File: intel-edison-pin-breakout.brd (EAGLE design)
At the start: 93.7 x 78.7 mm, 5 parts, among them U1 EDISON_CONNECTOR_FULLMOUNTING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

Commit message: put them closer
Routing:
- net N$33: track 56.3 -> 49.6 mm
- net N$1: track 55.5 -> 50.2 mm
- net N$32: track 53.1 -> 48.1 mm
- net N$2: track 52.4 -> 48.6 mm
- net N$31: track 50.3 -> 46.7 mm
- net N$3: track 49.5 -> 47.1 mm
- net N$30: track 46.9 -> 45.2 mm
- net N$4: track 46.8 -> 45.5 mm
- net N$5: track 44.8 -> 44.1 mm
- net N$29: track 44.5 -> 43.7 mm
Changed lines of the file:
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@@
 <contactref element="JP1" pad="1"/>
 <wire x1="40.52" y1="36.27" x2="40.518078125" y2="35.51681875" width="0.2032" layer="1"/>
-<wire x1="3.81" y1="3.81" x2="3.81" y2="17.78" width="0.2032" layer="1"/>
-<wire x1="3.81" y1="17.78" x2="40.518078125" y2="35.51681875" width="0.2032" layer="1"/>
+<wire x1="3.81" y1="3.81" x2="3.81" y2="6.35" width="0.2032" layer="1"/>
+<wire x1="3.81" y1="6.35" x2="40.518078125" y2="35.51681875" width="0.2032" layer="1"/>
 </signal>
 <signal name="N$2">
@@
 <contactref element="JP1" pad="2"/>
 <wire x1="40.92" y1="36.27" x2="40.9194" y2="35.304728125" width="0.2032" layer="1"/>
-<wire x1="6.35" y1="3.81" x2="6.35" y2="15.24" width="0.2032" layer="1"/>
-<wire x1="6.35" y1="15.24" x2="40.9194" y2="35.304728125" width="0.2032" layer="1"/>
+<wire x1="6.35" y1="3.81" x2="6.35" y2="6.35" width="0.2032" layer="1"/>
+<wire x1="6.35" y1="6.35" x2="40.9194" y2="35.304728125" width="0.2032" layer="1"/>
 </signal>
 <signal name="N$3">
@@
 <contactref element="JP1" pad="3"/>
 <wire x1="41.32" y1="36.27" x2="41.3169125" y2="35.05961875" width="0.2032" layer="1"/>
-<wire x1="8.89" y1="3.81" x2="8.89" y2="12.7" width="0.2032" layer="1"/>
-<wire x1="8.89" y1="12.7" x2="41.3169125" y2="35.05961875" width="0.2032" layer="1"/>
+<wire x1="8.89" y1="3.81" x2="8.89" y2="6.35" width="0.2032" layer="1"/>
+<wire x1="8.89" y1="6.35" x2="41.3169125" y2="35.05961875" width="0.2032" layer="1"/>
 </signal>
 <signal name="N$4">
@@
 <contactref element="JP1" pad="4"/>
 <wire x1="41.72" y1="36.27" x2="41.7068" y2="34.847528125" width="0.2032" layer="1"/>
-<wire x1="11.43" y1="3.81" x2="11.43" y2="10.16" width="0.2032" layer="1"/>
-<wire x1="11.43" y1="10.16" x2="41.7068" y2="34.847528125" width="0.2032" layer="1"/>
+<wire x1="11.43" y1="3.81" x2="11.43" y2="6.35" width="0.2032" layer="1"/>
+<wire x1="11.43" y1="6.35" x2="41.7068" y2="34.847528125" width="0.2032" layer="1"/>
 </signal>
 <signal name="N$5">
@@
 <contactref element="JP1" pad="5"/>
 <wire x1="42.12" y1="36.27" x2="42.1132" y2="34.671" width="0.2032" layer="1"/>
-<wire x1="13.97" y1="3.81" x2="13.97" y2="8.89" width="0.2032" layer="1"/>
-<wire x1="13.97" y1="8.89" x2="42.1132" y2="34.671" width="0.2032" layer="1"/>
+<wire x1="13.97" y1="3.81" x2="13.97" y2="6.35" width="0.2032" layer="1"/>
+<wire x1="13.97" y1="6.35" x2="42.1132" y2="34.671" width="0.2032" layer="1"/>
 </signal>
 <signal name="N$6">
 <contactref element="U1" pad="11"/>
 <contactref element="JP1" pad="6"/>
-<wire x1="16.51" y1="3.81" x2="16.51" y2="7.62" width="0.2032" layer="1"/>
+<wire x1="16.51" y1="3.81" x2="16.51" y2="6.35" width="0.2032" layer="1"/>
 <wire x1="42.52" y1="36.27" x2="42.503090625" y2="34.5059" width="0.2032" layer="1"/>
-<wire x1="42.503090625" y1="34.5059" x2="16.51" y2="7.62" width="0.2032" layer="1"/>
+<wire x1="42.503090625" y1="34.5059" x2="16.51" y2="6.35" width="0.2032" layer="1"/>
 </signal>
 <signal name="N$7">
@@
 <contactref element="JP2" pad="1"/>
 <wire x1="52.52" y1="36.27" x2="52.515771875" y2="34.189671875" width="0.2032" layer="1"/>
-<wire x1="80.01" y1="3.81" x2="80.01" y2="8.89" width="0.2032" layer="1"/>
-<wire x1="80.01" y1="8.89" x2="52.515771875" y2="34.189671875" width="0.2032" layer="1"/>
+<wire x1="80.01" y1="3.81" x2="80.01" y2="6.35" width="0.2032" layer="1"/>
+<wire x1="80.01" y1="6.35" x2="52.515771875" y2="34.189671875" width="0.2032" layer="1"/>
 </signal>
 <signal name="N$30">
@@
 <contactref element="JP2" pad="2"/>
 <wire x1="52.92" y1="36.27" x2="52.925978125" y2="34.4678" width="0.2032" layer="1"/>
-<wire x1="82.55" y1="3.81" x2="82.55" y2="11.43" width="0.2032" layer="1"/>
-<wire x1="52.925978125" y1="34.4678" x2="82.55" y2="11.43" width="0.2032" layer="1"/>
+<wire x1="82.55" y1="3.81" x2="82.55" y2="6.35" width="0.2032" layer="1"/>
+<wire x1="52.925978125" y1="34.4678" x2="82.55" y2="6.35" width="0.2032" layer="1"/>
 </signal>
 <signal name="N$31">
 <contactref element="U1" pad="65"/>
 <contactref element="JP2" pad="3"/>
-<wire x1="85.09" y1="3.81" x2="85.09" y2="15.24" width="0.2032" layer="1"/>
+<wire x1="85.09" y1="3.81" x2="85.09" y2="6.35" width="0.2032" layer="1"/>
 <wire x1="53.32" y1="36.27" x2="53.30570625" y2="34.72815" width="0.2032" layer="1"/>
-<wire x1="53.30570625" y1="34.72815" x2="85.09" y2="15.24" width="0.2032" layer="1"/>
+<wire x1="53.30570625" y1="34.72815" x2="85.09" y2="6.35" width="0.2032" layer="1"/>
 </signal>
 <signal name="N$32">
@@
 <contactref element="JP2" pad="4"/>
 <wire x1="53.72" y1="36.27" x2="53.73496875" y2="35.37076875" width="0.2032" layer="1"/>
-<wire x1="53.73496875" y1="35.37076875" x2="87.63" y2="17.78" width="0.2032" layer="1"/>
-<wire x1="87.63" y1="17.78" x2="87.63" y2="3.81" width="0.2032" layer="1"/>
+<wire x1="53.73496875" y1="35.37076875" x2="87.63" y2="6.35" width="0.2032" layer="1"/>
+<wire x1="87.63" y1="6.35" x2="87.63" y2="3.81" width="0.2032" layer="1"/>
 </signal>
 <signal name="N$33">
@@
 <contactref element="JP2" pad="5"/>
 <wire x1="54.12" y1="36.27" x2="54.12231875" y2="35.5727" width="0.2032" layer="1"/>
-<wire x1="54.12231875" y1="35.5727" x2="90.17" y2="20.32" width="0.2032" layer="1"/>
-<wire x1="90.17" y1="3.81" x2="90.17" y2="20.32" width="0.2032" layer="1"/>
+<wire x1="54.12231875" y1="35.5727" x2="90.17" y2="6.35" width="0.2032" layer="1"/>
+<wire x1="90.17" y1="3.81" x2="90.17" y2="6.35" width="0.2032" layer="1"/>
 </signal>
 <signal name="N$34">
@@
 <contactref element="JP1" pad="30"/>
 <wire x1="52.12" y1="36.27" x2="52.10936875" y2="33.917890625" width="0.2032" layer="1"/>
-<wire x1="77.47" y1="3.81" x2="77.47" y2="7.62" width="0.2032" layer="1"/>
-<wire x1="77.47" y1="7.62" x2="52.10936875" y2="33.917890625" width="0.2032" layer="1"/>
+<wire x1="77.47" y1="3.81" x2="77.47" y2="6.35" width="0.2032" layer="1"/>
+<wire x1="77.47" y1="6.35" x2="52.10936875" y2="33.917890625" width="0.2032" layer="1"/>
 </signal>
 <signal name="N$20">

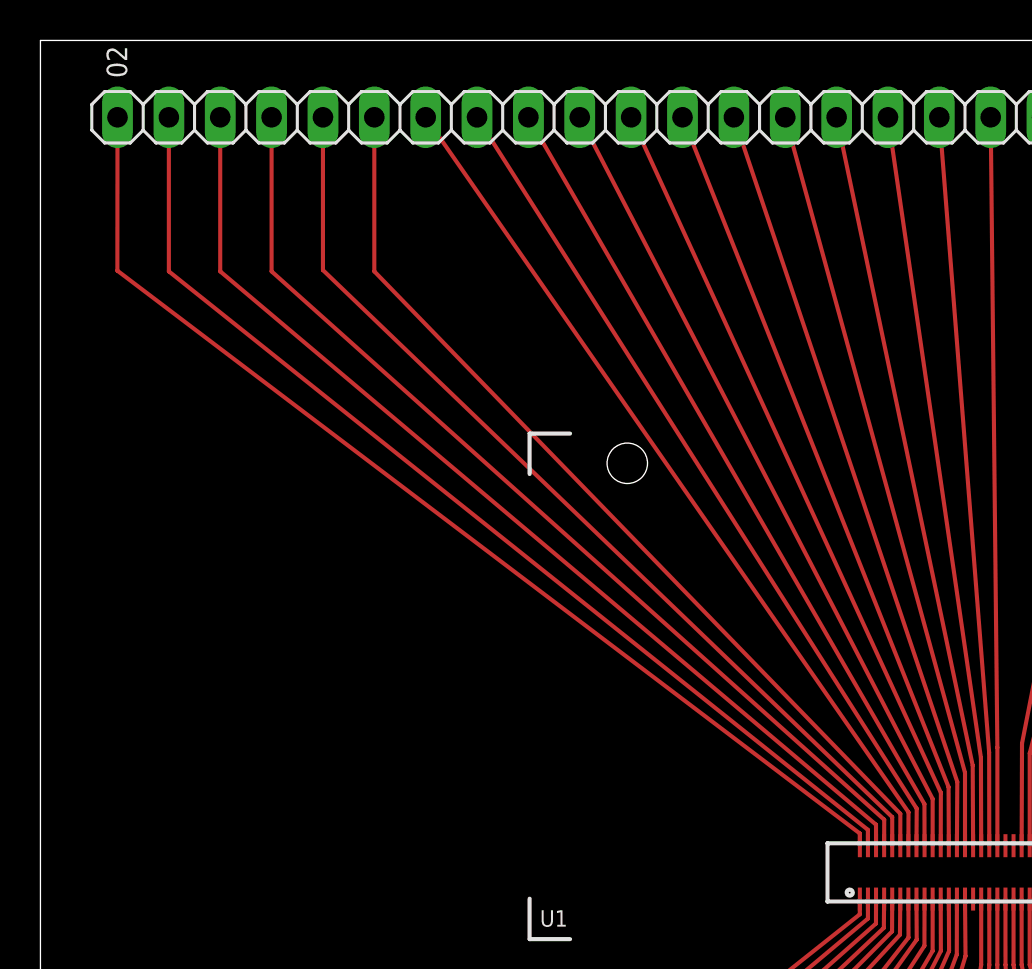
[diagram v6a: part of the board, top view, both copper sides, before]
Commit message: all pins fit on smaller board
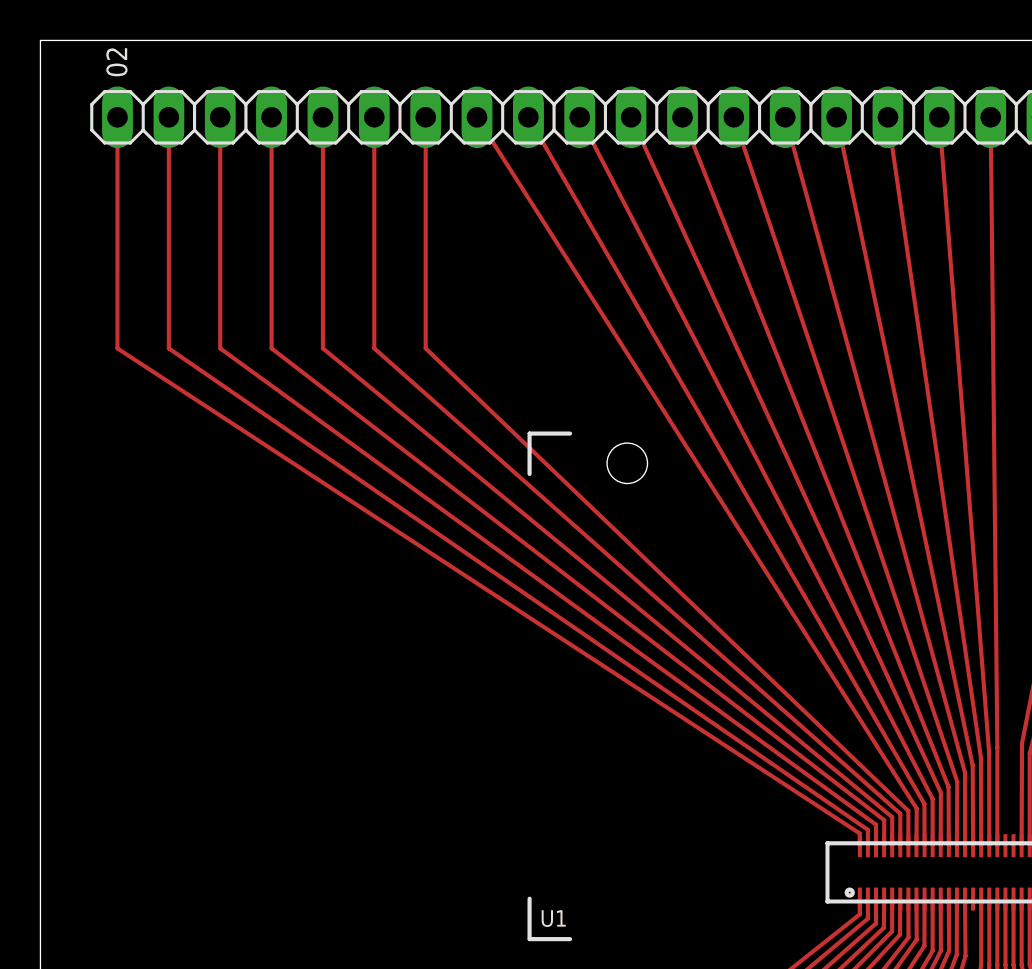
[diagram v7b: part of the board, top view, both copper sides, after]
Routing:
- net N$40: track 43.5 -> 46.2 mm
- net N$34: track 54.3 -> 55.9 mm
- net N$35: track 52.6 -> 54.2 mm
- net N$36: track 51.1 -> 52.5 mm
- net N$37: track 49.6 -> 50.9 mm
- net N$38: track 48.0 -> 49.3 mm
- net N$39: track 46.6 -> 47.7 mm
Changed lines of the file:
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@@
 <contactref element="JP3" pad="1"/>
 <wire x1="40.52" y1="38.91" x2="40.521890625" y2="39.512240625" width="0.2032" layer="1"/>
-<wire x1="40.521890625" y1="39.512240625" x2="3.803759375" y2="67.34555625" width="0.2032" layer="1"/>
-<wire x1="3.81" y1="74.93" x2="3.803759375" y2="67.34555625" width="0.2032" layer="1"/>
+<wire x1="40.521890625" y1="39.512240625" x2="3.80884375" y2="63.5" width="0.2032" layer="1"/>
+<wire x1="3.81" y1="74.93" x2="3.80884375" y2="63.5" width="0.2032" layer="1"/>
 </signal>
 <signal name="N$35">
 <contactref element="U1" pad="4"/>
 <contactref element="JP3" pad="2"/>
-<wire x1="6.35" y1="74.93" x2="6.35" y2="67.31" width="0.2032" layer="1"/>
+<wire x1="6.35" y1="74.93" x2="6.35" y2="63.5" width="0.2032" layer="1"/>
 <wire x1="40.92" y1="38.91" x2="40.91813125" y2="39.69511875" width="0.2032" layer="1"/>
-<wire x1="40.91813125" y1="39.69511875" x2="6.35" y2="67.31" width="0.2032" layer="1"/>
+<wire x1="40.91813125" y1="39.69511875" x2="6.35" y2="63.5" width="0.2032" layer="1"/>
 </signal>
 <signal name="N$36">
 <contactref element="U1" pad="6"/>
 <contactref element="JP3" pad="3"/>
-<wire x1="8.89" y1="74.93" x2="8.89" y2="67.31" width="0.2032" layer="1"/>
+<wire x1="8.89" y1="74.93" x2="8.89" y2="63.5" width="0.2032" layer="1"/>
 <wire x1="41.32" y1="38.91" x2="41.31945" y2="39.950390625" width="0.2032" layer="1"/>
-<wire x1="41.31945" y1="39.950390625" x2="8.89" y2="67.31" width="0.2032" layer="1"/>
+<wire x1="41.31945" y1="39.950390625" x2="8.89" y2="63.5" width="0.2032" layer="1"/>
 </signal>
 <signal name="N$37">
 <contactref element="U1" pad="8"/>
 <contactref element="JP3" pad="4"/>
-<wire x1="11.43" y1="74.93" x2="11.43" y2="67.31" width="0.2032" layer="1"/>
-<wire x1="41.72" y1="38.91" x2="41.72585" y2="40.19676875" width="0.2032" layer="1"/>
-<wire x1="41.72585" y1="40.19676875" x2="11.43" y2="67.31" width="0.2032" layer="1"/>
+<wire x1="11.43" y1="74.93" x2="11.43" y2="63.5" width="0.2032" layer="1"/>
+<wire x1="41.72" y1="38.91" x2="41.72585" y2="40.1726375" width="0.2032" layer="1"/>
+<wire x1="41.72585" y1="40.1726375" x2="11.43" y2="63.5" width="0.2032" layer="1"/>
 </signal>
 <signal name="N$38">
@@
 <wire x1="42.12" y1="38.91" x2="42.11828125" y2="38.91" width="0.2032" layer="1"/>
 <wire x1="42.12" y1="38.91" x2="42.12081875" y2="40.325040625" width="0.2032" layer="1"/>
-<wire x1="13.97" y1="67.37223125" x2="13.97" y2="74.93" width="0.2032" layer="1"/>
-<wire x1="42.12081875" y1="40.325040625" x2="13.97" y2="67.37223125" width="0.2032" layer="1"/>
+<wire x1="13.97" y1="63.5" x2="13.97" y2="74.93" width="0.2032" layer="1"/>
+<wire x1="42.12081875" y1="40.325040625" x2="13.97" y2="63.5" width="0.2032" layer="1"/>
 </signal>
 <signal name="N$39">
@@
 <contactref element="JP3" pad="6"/>
 <wire x1="42.52" y1="38.91" x2="42.522140625" y2="40.48886875" width="0.2032" layer="1"/>
-<wire x1="16.51" y1="74.93" x2="16.51" y2="67.31" width="0.2032" layer="1"/>
-<wire x1="16.51" y1="67.31" x2="42.522140625" y2="40.48886875" width="0.2032" layer="1"/>
+<wire x1="16.51" y1="74.93" x2="16.51" y2="63.5" width="0.2032" layer="1"/>
+<wire x1="16.51" y1="63.5" x2="42.522140625" y2="40.48886875" width="0.2032" layer="1"/>
 </signal>
 <signal name="N$40">
 <contactref element="U1" pad="14"/>
 <contactref element="JP3" pad="7"/>
-<wire x1="42.92" y1="38.91" x2="42.926" y2="40.5638" width="0.2032" layer="1"/>
-<wire x1="42.926" y1="40.5638" x2="19.05" y2="74.93" width="0.2032" layer="1"/>
+<wire x1="42.92" y1="38.91" x2="42.91838125" y2="40.627296875" width="0.2032" layer="1"/>
+<wire x1="19.05" y1="74.93" x2="19.05" y2="63.5" width="0.2032" layer="1"/>
+<wire x1="19.05" y1="63.5" x2="42.91838125" y2="40.627296875" width="0.2032" layer="1"/>
 </signal>
 <signal name="N$41">
